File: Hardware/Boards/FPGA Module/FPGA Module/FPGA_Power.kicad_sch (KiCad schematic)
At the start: 1 part, among them U1 XCKU3P-FFVA676

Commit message: Added FPGA Config page
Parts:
- removed U1: XCKU3P-FFVA676, DICE_FPGA_Module:BGA676, symbol DICE_FPGA_Module:XCKU3P-FFVA676
- added U1: XCKU3P-FFVA676, FPGA Module:BGA676, symbol FPGA Module:XCKU3P-FFVA676
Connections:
- new net: U1.AD10 (NC), U1.AE13 (NC), U1.E24 (NC), U1.E25 (NC), U1.E26 (NC), U1.F22 (NC), U1.F23 (NC), U1.F24 (NC), U1.F25 (NC), U1.G20 (NC), U1.G21 (NC), U1.G22 (NC), U1.G24 (NC), U1.G25 (NC), U1.G26 (NC), U1.H19 (NC), U1.H21 (NC), U1.H22 (NC), U1.H23 (NC), U1.H24 (NC), U1.H25 (NC), U1.H26 (NC), U1.J19 (NC), U1.J20 (NC), U1.J21 (NC), U1.J22 (NC), U1.J23 (NC), U1.J24 (NC), U1.J25 (NC), U1.J26 (NC), U1.K18 (NC), U1.K19 (NC), U1.K20 (NC), U1.K21 (NC), U1.K22 (NC), U1.K23 (NC), U1.K25 (NC), U1.K26 (NC), U1.L18 (NC), U1.L19 (NC), U1.L20 (NC), U1.L22 (NC), U1.L23 (NC), U1.L24 (NC), U1.L25 (NC), U1.L26 (NC), U1.M19 (NC), U1.M20 (NC), U1.M21 (NC), U1.M22 (NC), U1.M23 (NC), U1.M24 (NC), U1.M25 (NC), U1.M26 (NC), U1.N18 (NC), U1.N19 (NC), U1.N20 (NC), U1.N21 (NC), U1.N22 (NC), U1.N23 (NC), U1.N24 (NC), U1.N26 (NC), U1.V14 (NC), U1.Y12 (NC), U1.Y13 (NC)
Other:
- note added: "HDMI"

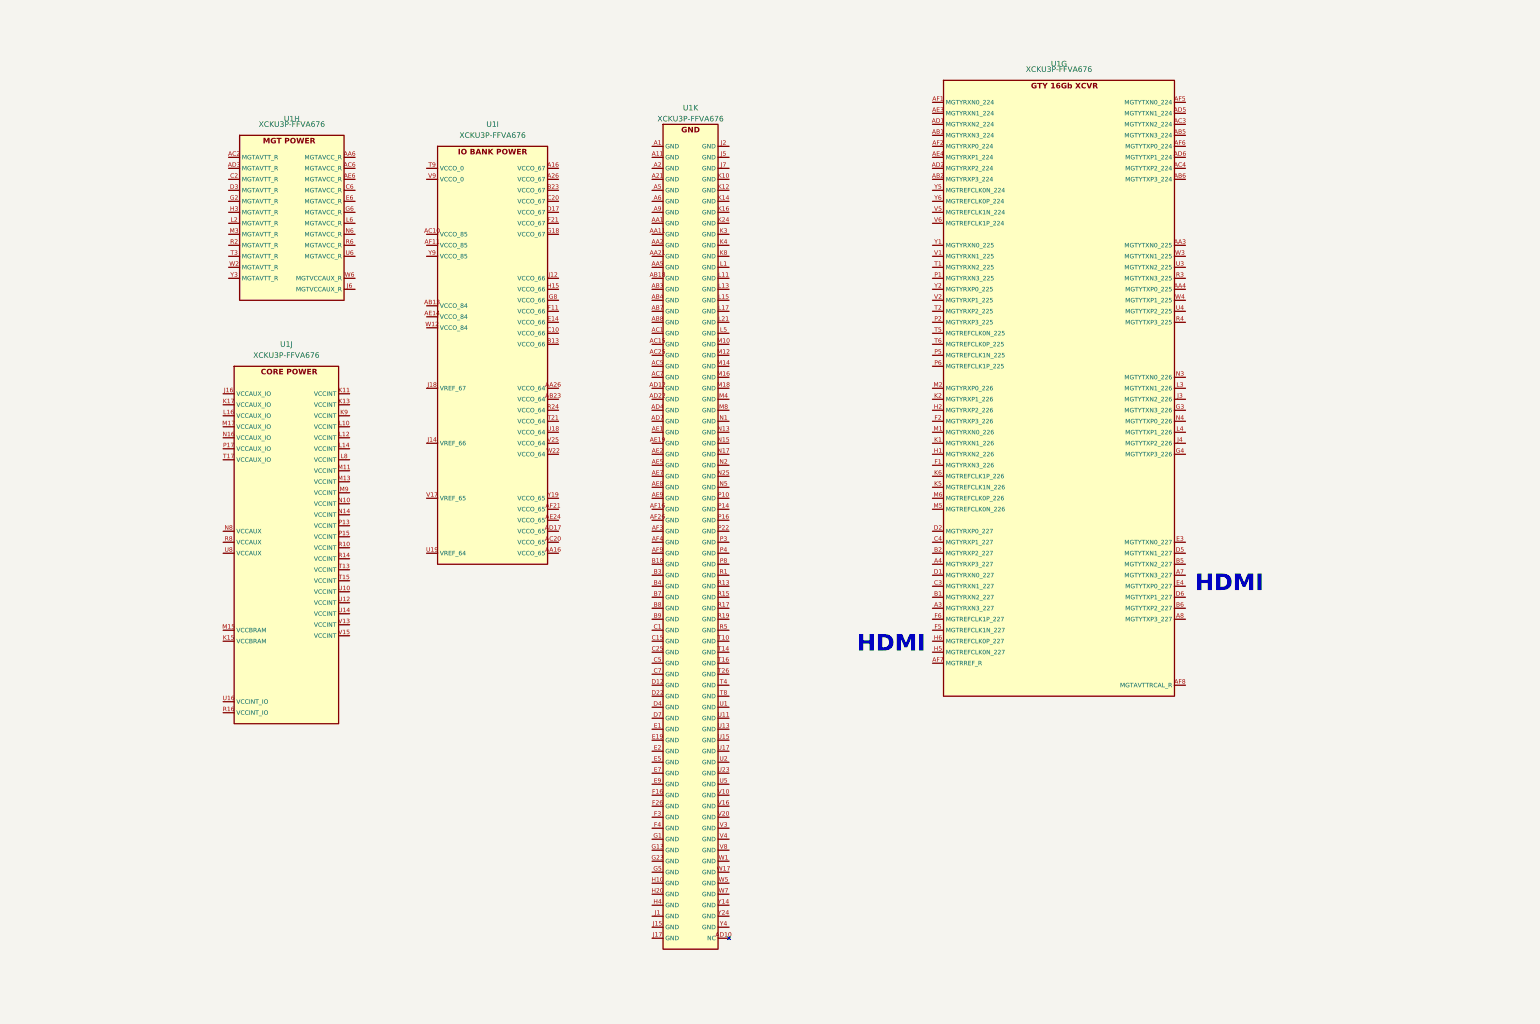
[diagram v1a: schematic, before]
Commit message: Using new DP to HDMI IC
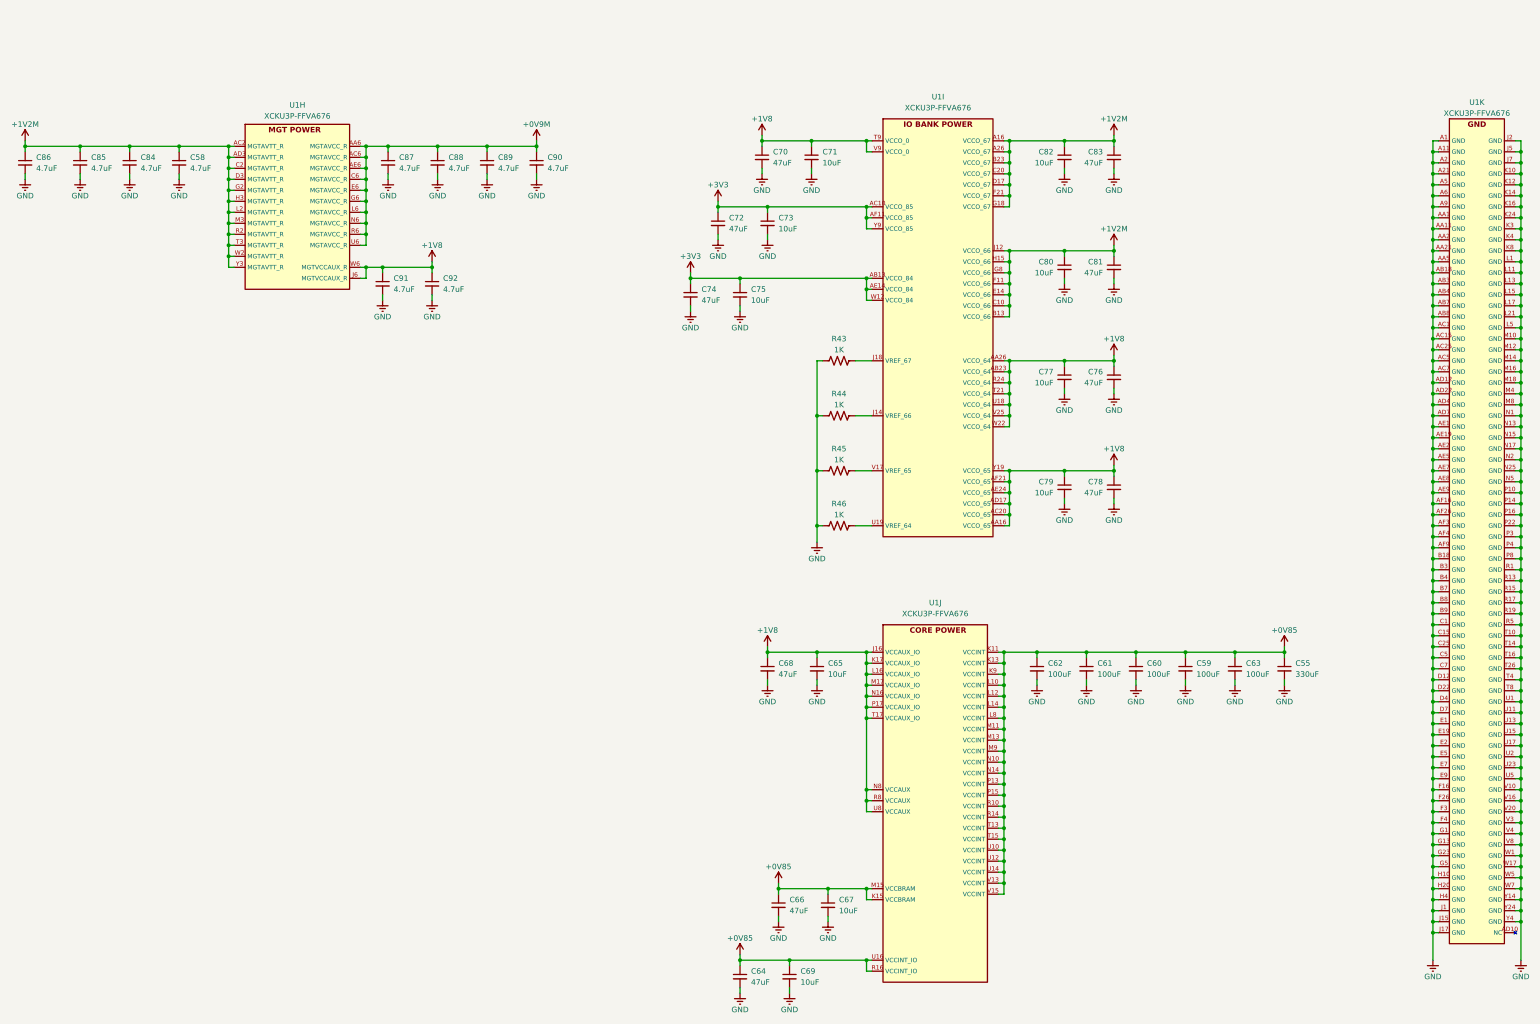
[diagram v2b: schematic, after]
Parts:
- removed unit 7 of U1
- added C55: 330uF, Capacitor_SMD:C_1210_3225Metric, symbol Device:C_Small
- added C58, C84, C85, C86, C87, C88, C89, C90, C91, C92: 4.7uF, Capacitor_SMD:C_0402_1005Metric, symbol Device:C_Small
- added C59, C60, C61, C62, C63: 100uF, Capacitor_SMD:C_0805_2012Metric, symbol Device:C_Small
- added C64, C66, C68, C70, C72, C74, C76, C78, C81, C83: 47uF, Capacitor_SMD:C_0603_1608Metric, symbol Device:C_Small
- added C65, C67, C69, C71, C73, C75, C77, C79, C80, C82: 10uF, Capacitor_SMD:C_0402_1005Metric, symbol Device:C_Small
- added R43, R44, R45, R46: 1K, Resistor_SMD:R_0402_1005Metric, symbol Device:R_US
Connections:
- net +1V2M: now reaches U1.A16 (VCCO_67)
- net +1V2M: now also U1.A26 (VCCO_67), U1.AC2 (MGTAVTT_R), U1.AD3 (MGTAVTT_R), U1.B13 (VCCO_66), U1.B23 (VCCO_67), U1.C10 (VCCO_66), U1.C2 (MGTAVTT_R), U1.C20 (VCCO_67), U1.D17 (VCCO_67), U1.D3 (MGTAVTT_R), U1.E14 (VCCO_66), U1.F11 (VCCO_66), U1.F21 (VCCO_67), U1.G18 (VCCO_67), U1.G2 (MGTAVTT_R), U1.G8 (VCCO_66), U1.H15 (VCCO_66), U1.H3 (MGTAVTT_R), U1.J12 (VCCO_66), U1.L2 (MGTAVTT_R), U1.M3 (MGTAVTT_R), U1.R2 (MGTAVTT_R), U1.T3 (MGTAVTT_R), U1.W2 (MGTAVTT_R), U1.Y3 (MGTAVTT_R), C58.1, C80.1, C81.1, C82.1, C83.1, C84.1, C85.1, C86.1
- net +1V8: now reaches U1.AA16 (VCCO_65)
- net +1V8: now also U1.AA26 (VCCO_64), U1.AB23 (VCCO_64), U1.AC20 (VCCO_65), U1.AD17 (VCCO_65), U1.AE24 (VCCO_65), U1.AF21 (VCCO_65), U1.J16 (VCCAUX_IO), U1.J6 (MGTVCCAUX_R), U1.K17 (VCCAUX_IO), U1.L16 (VCCAUX_IO), U1.M17 (VCCAUX_IO), U1.N16 (VCCAUX_IO), U1.N8 (VCCAUX), U1.P17 (VCCAUX_IO), U1.R24 (VCCO_64), U1.R8 (VCCAUX), U1.T17 (VCCAUX_IO), U1.T21 (VCCO_64), U1.T9 (VCCO_0), U1.U18 (VCCO_64), U1.U8 (VCCAUX), U1.V25 (VCCO_64), U1.V9 (VCCO_0), U1.W22 (VCCO_64), U1.W6 (MGTVCCAUX_R), U1.Y19 (VCCO_65), C65.1, C68.1, C70.1, C71.1, C76.1, C77.1, C78.1, C79.1, C91.1, C92.1
- net +3V3: now reaches U1.AB13 (VCCO_84)
- net +3V3: now also U1.AC10 (VCCO_85), U1.AE14 (VCCO_84), U1.AF11 (VCCO_85), U1.W12 (VCCO_84), U1.Y9 (VCCO_85), C72.1, C73.1, C74.1, C75.1
- net at U1.J14 (VREF_66): now also R44.1
- net at U1.J18 (VREF_67): now also R43.1
- net at U1.U19 (VREF_64): now also R46.1
- net at U1.V17 (VREF_65): now also R45.1
- net +0V85: now reaches U1.K11 (VCCINT)
- net +0V85: now also U1.K13 (VCCINT), U1.K15 (VCCBRAM), U1.K9 (VCCINT), U1.L10 (VCCINT), U1.L12 (VCCINT), U1.L14 (VCCINT), U1.L8 (VCCINT), U1.M11 (VCCINT), U1.M13 (VCCINT), U1.M15 (VCCBRAM), U1.M9 (VCCINT), U1.N10 (VCCINT), U1.N14 (VCCINT), U1.P13 (VCCINT), U1.P15 (VCCINT), U1.R10 (VCCINT), U1.R14 (VCCINT), U1.R16 (VCCINT_IO), U1.T13 (VCCINT), U1.T15 (VCCINT), U1.U10 (VCCINT), U1.U12 (VCCINT), U1.U14 (VCCINT), U1.U16 (VCCINT_IO), U1.V13 (VCCINT), U1.V15 (VCCINT), C55.1, C59.1, C60.1, C61.1, C62.1, C63.1, C64.1, C66.1, C67.1, C69.1
- net GND: now reaches U1.A1 (GND)
- net GND: now also U1.A11 (GND), U1.A2 (GND), U1.A21 (GND), U1.A5 (GND), U1.A6 (GND), U1.A9 (GND), U1.AA1 (GND), U1.AA11 (GND), U1.AA2 (GND), U1.AA21 (GND), U1.AA5 (GND), U1.AB18 (GND), U1.AB3 (GND), U1.AB4 (GND), U1.AB7 (GND), U1.AB8 (GND), U1.AC1 (GND), U1.AC15 (GND), U1.AC25 (GND), U1.AC5 (GND), U1.AC7 (GND), U1.AD12 (GND), U1.AD22 (GND), U1.AD4 (GND), U1.AD7 (GND), U1.AE1 (GND), U1.AE19 (GND), U1.AE2 (GND), U1.AE5 (GND), U1.AE7 (GND), U1.AE8 (GND), U1.AE9 (GND), U1.AF16 (GND), U1.AF26 (GND), U1.AF3 (GND), U1.AF4 (GND), U1.AF9 (GND), U1.B18 (GND), U1.B3 (GND), U1.B4 (GND), U1.B7 (GND), U1.B8 (GND), U1.B9 (GND), U1.C1 (GND), U1.C15 (GND), U1.C25 (GND), U1.C5 (GND), U1.C7 (GND), U1.D12 (GND), U1.D22 (GND), U1.D4 (GND), U1.D7 (GND), U1.E1 (GND), U1.E19 (GND), U1.E2 (GND), U1.E5 (GND), U1.E7 (GND), U1.E9 (GND), U1.F16 (GND), U1.F26 (GND), U1.F3 (GND), U1.F4 (GND), U1.G1 (GND), U1.G13 (GND), U1.G23 (GND), U1.G5 (GND), U1.H10 (GND), U1.H20 (GND), U1.H4 (GND), U1.J1 (GND), U1.J15 (GND), U1.J17 (GND), U1.J2 (GND), U1.J5 (GND), U1.J7 (GND), U1.K10 (GND), U1.K12 (GND), U1.K14 (GND), U1.K16 (GND), U1.K24 (GND), U1.K3 (GND), U1.K4 (GND), U1.K8 (GND), U1.L1 (GND), U1.L11 (GND), U1.L13 (GND), U1.L15 (GND), U1.L17 (GND), U1.L21 (GND), U1.L5 (GND), U1.M10 (GND), U1.M12 (GND), U1.M14 (GND), U1.M16 (GND), U1.M18 (GND), U1.M4 (GND), U1.M8 (GND), U1.N1 (GND), U1.N13 (GND), U1.N15 (GND), U1.N17 (GND), U1.N2 (GND), U1.N25 (GND), U1.N5 (GND), U1.P10 (GND), U1.P14 (GND), U1.P16 (GND), U1.P22 (GND), U1.P3 (GND), U1.P4 (GND), U1.P8 (GND), U1.R1 (GND), U1.R13 (GND), U1.R15 (GND), U1.R17 (GND), U1.R19 (GND), U1.R5 (GND), U1.T10 (GND), U1.T14 (GND), U1.T16 (GND), U1.T26 (GND), U1.T4 (GND), U1.T8 (GND), U1.U1 (GND), U1.U11 (GND), U1.U13 (GND), U1.U15 (GND), U1.U17 (GND), U1.U2 (GND), U1.U23 (GND), U1.U5 (GND), U1.V10 (GND), U1.V16 (GND), U1.V20 (GND), U1.V3 (GND), U1.V4 (GND), U1.V8 (GND), U1.W1 (GND), U1.W17 (GND), U1.W5 (GND), U1.W7 (GND), U1.Y14 (GND), U1.Y24 (GND), U1.Y4 (GND), C55.2, C58.2, C59.2, C60.2, C61.2, C62.2, C63.2, C64.2, C65.2, C66.2, C67.2, C68.2, C69.2, C70.2, C71.2, C72.2, C73.2, C74.2, C75.2, C76.2, C77.2, C78.2, C79.2, C80.2, C81.2, C82.2, C83.2, C84.2, C85.2, C86.2, C87.2, C88.2, C89.2, C90.2, C91.2, C92.2, R43.2, R44.2, R45.2, R46.2
- net +0V9M: now reaches U1.AA6 (MGTAVCC_R)
- net +0V9M: now also U1.AC6 (MGTAVCC_R), U1.AE6 (MGTAVCC_R), U1.C6 (MGTAVCC_R), U1.E6 (MGTAVCC_R), U1.G6 (MGTAVCC_R), U1.L6 (MGTAVCC_R), U1.N6 (MGTAVCC_R), U1.R6 (MGTAVCC_R), U1.U6 (MGTAVCC_R), C87.1, C88.1, C89.1, C90.1
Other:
- note removed: "HDMI"
- moved on the sheet: U1H, U1I, U1J, U1K

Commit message: updated fpga module schematics
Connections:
- net +0V9M renamed +0V9
- net +1V2M renamed +1V2
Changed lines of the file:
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@@
 		(rev "1.0")
 		(company "Drexel University")
-		(comment 1 "Designed by Michael Haahr")
+		(comment 1 "Designed by John Hofmeyr")
 	)
 	(junction
@@
 	)
 	(symbol
-		(lib_id "power:GND")
-		(at 53.34 54.61 0)
+		(lib_id "power:+1V2")
+		(at 280.67 44.45 0)
 		(unit 1)
 		(exclude_from_sim no)
@@
 		(on_board yes)
 		(dnp no)
-		(property "Reference" "#PWR0150"
-			(at 53.34 60.96 0)
+		(property "Reference" "#PWR0117"
+			(at 280.67 48.26 0)
 			(effects
 				(font
@@
 			)
 		)
-		(property "Value" "GND"
-			(at 53.34 58.42 0)
+		(property "Value" "+1V2"
+			(at 280.67 40.64 0)
 			(effects
 				(font
@@
 		)
 		(property "Footprint" ""
-			(at 53.34 54.61 0)
+			(at 280.67 44.45 0)
 			(effects
 				(font
@@
 		)
 		(property "Datasheet" ""
-			(at 53.34 54.61 0)
+			(at 280.67 44.45 0)
 			(effects
 				(font
@@
 			)
 		)
-		(property "Description" "Power symbol creates a global label with name \"GND\" , ground"
-			(at 53.34 54.61 0)
+		(property "Description" "Power symbol creates a global label with name \"+1V2\""
+			(at 280.67 44.45 0)
 			(effects
 				(font
@@
 			(project "FPGA Module"
 				(path "/199f10e2-d4b4-4a27-9e84-7b1ce2ae6bf0/0c296310-f788-47f0-8a3f-43c3444563e8/ff43e174-bde2-43ac-b61b-dc2c71092798"
-					(reference "#PWR0150")
+					(reference "#PWR0117")
 					(unit 1)
 				)
@@
 	)
 	(symbol
-		(lib_id "power:VAA")
-		(at 147.32 45.72 0)
+		(lib_id "power:GND")
+		(at 53.34 54.61 0)
 		(unit 1)
 		(exclude_from_sim no)
@@
 		(on_board yes)
 		(dnp no)
-		(property "Reference" "#PWR0117"
-			(at 147.32 49.53 0)
+		(property "Reference" "#PWR0150"
+			(at 53.34 60.96 0)
 			(effects
 				(font
@@
 			)
 		)
-		(property "Value" "+0V9M"
-			(at 147.32 41.91 0)
+		(property "Value" "GND"
+			(at 53.34 58.42 0)
 			(effects
 				(font
@@
 		)
 		(property "Footprint" ""
-			(at 147.32 45.72 0)
+			(at 53.34 54.61 0)
 			(effects
 				(font
@@
 		)
 		(property "Datasheet" ""
-			(at 147.32 45.72 0)
+			(at 53.34 54.61 0)
 			(effects
 				(font
@@
 			)
 		)
-		(property "Description" "Power symbol creates a global label with name \"VAA\""
-			(at 147.32 45.72 0)
+		(property "Description" "Power symbol creates a global label with name \"GND\" , ground"
+			(at 53.34 54.61 0)
 			(effects
 				(font
@@
 			(project "FPGA Module"
 				(path "/199f10e2-d4b4-4a27-9e84-7b1ce2ae6bf0/0c296310-f788-47f0-8a3f-43c3444563e8/ff43e174-bde2-43ac-b61b-dc2c71092798"
-					(reference "#PWR0117")
+					(reference "#PWR0150")
 					(unit 1)
 				)
@@
 	(symbol
 		(lib_id "power:VAA")
-		(at 280.67 69.85 0)
+		(at 147.32 45.72 0)
 		(unit 1)
 		(exclude_from_sim no)
@@
 		(on_board yes)
 		(dnp no)
-		(property "Reference" "#PWR0141"
-			(at 280.67 73.66 0)
+		(property "Reference" "#PWR0257"
+			(at 147.32 49.53 0)
 			(effects
 				(font
@@
 			)
 		)
-		(property "Value" "+1V2M"
-			(at 280.67 66.04 0)
+		(property "Value" "+0V9"
+			(at 147.32 41.91 0)
 			(effects
 				(font
@@
 		)
 		(property "Footprint" ""
-			(at 280.67 69.85 0)
+			(at 147.32 45.72 0)
 			(effects
 				(font
@@
 		)
 		(property "Datasheet" ""
-			(at 280.67 69.85 0)
+			(at 147.32 45.72 0)
 			(effects
 				(font
@@
 		)
 		(property "Description" "Power symbol creates a global label with name \"VAA\""
-			(at 280.67 69.85 0)
+			(at 147.32 45.72 0)
 			(effects
 				(font
@@
 			(project "FPGA Module"
 				(path "/199f10e2-d4b4-4a27-9e84-7b1ce2ae6bf0/0c296310-f788-47f0-8a3f-43c3444563e8/ff43e174-bde2-43ac-b61b-dc2c71092798"
-					(reference "#PWR0141")
+					(reference "#PWR0257")
 					(unit 1)
 				)
@@
 	)
 	(symbol
+		(lib_id "power:+1V2")
+		(at 280.67 69.85 0)
+		(unit 1)
+		(exclude_from_sim no)
+		(in_bom yes)
+		(on_board yes)
+		(dnp no)
+		(property "Reference" "#PWR0141"
+			(at 280.67 73.66 0)
+			(effects
+				(font
+					(size 1.27 1.27)
+				)
+				(hide yes)
+			)
+		)
+		(property "Value" "+1V2"
+			(at 280.67 66.04 0)
+			(effects
+				(font
+					(size 1.27 1.27)
+				)
+			)
+		)
+		(property "Footprint" ""
+			(at 280.67 69.85 0)
+			(effects
+				(font
+					(size 1.27 1.27)
+				)
+				(hide yes)
+			)
+		)
+		(property "Datasheet" ""
+			(at 280.67 69.85 0)
+			(effects
+				(font
+					(size 1.27 1.27)
+				)
+				(hide yes)
+			)
+		)
+		(property "Description" "Power symbol creates a global label with name \"+1V2\""
+			(at 280.67 69.85 0)
+			(effects
+				(font
+					(size 1.27 1.27)
+				)
+				(hide yes)
+			)
+		)
+		(pin "1"
+		)
+		(instances
+			(project "FPGA Module"
+				(path "/199f10e2-d4b4-4a27-9e84-7b1ce2ae6bf0/0c296310-f788-47f0-8a3f-43c3444563e8/ff43e174-bde2-43ac-b61b-dc2c71092798"
+					(reference "#PWR0141")
+					(unit 1)
+				)
+			)
+		)
+	)
+	(symbol
 		(lib_id "Device:C_Small")
 		(at 212.09 167.64 0)
@@
 	)
 	(symbol
-		(lib_id "power:GND")
-		(at 41.91 54.61 0)
+		(lib_id "power:+1V2")
+		(at 29.21 45.72 0)
 		(unit 1)
 		(exclude_from_sim no)
@@
 		(on_board yes)
 		(dnp no)
-		(property "Reference" "#PWR0148"
-			(at 41.91 60.96 0)
+		(property "Reference" "#PWR0119"
+			(at 29.21 49.53 0)
 			(effects
 				(font
@@
 			)
 		)
-		(property "Value" "GND"
-			(at 41.91 58.42 0)
+		(property "Value" "+1V2"
+			(at 29.21 41.91 0)
 			(effects
 				(font
@@
 		)
 		(property "Footprint" ""
-			(at 41.91 54.61 0)
+			(at 29.21 45.72 0)
 			(effects
 				(font
@@
 		)
 		(property "Datasheet" ""
-			(at 41.91 54.61 0)
+			(at 29.21 45.72 0)
 			(effects
 				(font
@@
 			)
 		)
-		(property "Description" "Power symbol creates a global label with name \"GND\" , ground"
-			(at 41.91 54.61 0)
+		(property "Description" "Power symbol creates a global label with name \"+1V2\""
+			(at 29.21 45.72 0)
 			(effects
 				(font
@@
 			(project "FPGA Module"
 				(path "/199f10e2-d4b4-4a27-9e84-7b1ce2ae6bf0/0c296310-f788-47f0-8a3f-43c3444563e8/ff43e174-bde2-43ac-b61b-dc2c71092798"
-					(reference "#PWR0148")
+					(reference "#PWR0119")
 					(unit 1)
 				)
@@
 	)
 	(symbol
-		(lib_id "power:VAA")
-		(at 280.67 44.45 0)
+		(lib_id "power:GND")
+		(at 41.91 54.61 0)
 		(unit 1)
 		(exclude_from_sim no)
@@
 		(on_board yes)
 		(dnp no)
-		(property "Reference" "#PWR0144"
-			(at 280.67 48.26 0)
+		(property "Reference" "#PWR0148"
+			(at 41.91 60.96 0)
 			(effects
 				(font
@@
 			)
 		)
-		(property "Value" "+1V2M"
-			(at 280.67 40.64 0)
+		(property "Value" "GND"
+			(at 41.91 58.42 0)
 			(effects
 				(font
@@
 		)
 		(property "Footprint" ""
-			(at 280.67 44.45 0)
+			(at 41.91 54.61 0)
 			(effects
 				(font
@@
 		)
 		(property "Datasheet" ""
-			(at 280.67 44.45 0)
+			(at 41.91 54.61 0)
 			(effects
 				(font
@@
 			)
 		)
-		(property "Description" "Power symbol creates a global label with name \"VAA\""
-			(at 280.67 44.45 0)
+		(property "Description" "Power symbol creates a global label with name \"GND\" , ground"
+			(at 41.91 54.61 0)
 			(effects
 				(font
@@
 			(project "FPGA Module"
 				(path "/199f10e2-d4b4-4a27-9e84-7b1ce2ae6bf0/0c296310-f788-47f0-8a3f-43c3444563e8/ff43e174-bde2-43ac-b61b-dc2c71092798"
-					(reference "#PWR0144")
+					(reference "#PWR0148")
 					(unit 1)
 				)
@@
 					(unit 1)
 				)
-			)
-		)
-	)
-	(symbol
-		(lib_id "power:VAA")
-		(at 29.21 45.72 0)
-		(unit 1)
-		(exclude_from_sim no)
-		(in_bom yes)
-		(on_board yes)
-		(dnp no)
-		(property "Reference" "#PWR0119"
-			(at 29.21 49.53 0)
-			(effects
-				(font
-					(size 1.27 1.27)
-				)
-				(hide yes)
-			)
-		)
-		(property "Value" "+1V2M"
-			(at 29.21 41.91 0)
-			(effects
-				(font
-					(size 1.27 1.27)
-				)
-			)
-		)
-		(property "Footprint" ""
-			(at 29.21 45.72 0)
-			(effects
-				(font
-					(size 1.27 1.27)
-				)
-				(hide yes)
-			)
-		)
-		(property "Datasheet" ""
-			(at 29.21 45.72 0)
-			(effects
-				(font
-					(size 1.27 1.27)
-				)
-				(hide yes)
-			)
-		)
-		(property "Description" "Power symbol creates a global label with name \"VAA\""
-			(at 29.21 45.72 0)
-			(effects
-				(font
-					(size 1.27 1.27)
-				)
-				(hide yes)
-			)
-		)
-		(pin "1"
-		)
-		(instances
-			(project "FPGA Module"
-				(path "/199f10e2-d4b4-4a27-9e84-7b1ce2ae6bf0/0c296310-f788-47f0-8a3f-43c3444563e8/ff43e174-bde2-43ac-b61b-dc2c71092798"
-					(reference "#PWR0119")
-					(unit 1)
-				)

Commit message: Update FPGA Module Netclasses
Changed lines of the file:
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@@
 		)
 	)
-	(symbol
-		(lib_id "power:GND")
-		(at 354.33 234.95 0)
-		(unit 1)
-		(exclude_from_sim no)
-		(in_bom yes)
-		(on_board yes)
-		(dnp no)
-		(property "Reference" "#PWR0106"
-			(at 354.33 241.3 0)
-			(effects
-				(font
-					(size 1.27 1.27)
-				)
-				(hide yes)
-			)
-		)
-		(property "Value" "GND"
-			(at 354.33 238.76 0)
-			(effects
-				(font
-					(size 1.27 1.27)
-				)
-			)
-		)
-		(property "Footprint" ""
-			(at 354.33 234.95 0)
-			(effects
-				(font
-					(size 1.27 1.27)
-				)
-				(hide yes)
-			)
-		)
-		(property "Datasheet" ""
-			(at 354.33 234.95 0)
-			(effects
-				(font
-					(size 1.27 1.27)
-				)
-				(hide yes)
-			)
-		)
-		(property "Description" "Power symbol creates a global label with name \"GND\" , ground"
-			(at 354.33 234.95 0)
-			(effects
-				(font
-					(size 1.27 1.27)
-				)
-				(hide yes)
-			)
-		)
-		(pin "1"
-		)
-		(instances
-			(project "FPGA Module"
-				(path "/199f10e2-d4b4-4a27-9e84-7b1ce2ae6bf0/0c296310-f788-47f0-8a3f-43c3444563e8/ff43e174-bde2-43ac-b61b-dc2c71092798"
-					(reference "#PWR0106")
-					(unit 1)
-				)
+	(label "GND"
+		(at 354.33 233.68 90)
+		(fields_autoplaced yes)
+		(effects
+			(font
+				(size 1.27 1.27)
 			)
+			(justify left bottom)
 		)
 	)
@@
 	)
 	(symbol
-		(lib_id "power:GND")
-		(at 212.09 138.43 0)
-		(mirror y)
-		(unit 1)
-		(exclude_from_sim no)
-		(in_bom yes)
-		(on_board yes)
-		(dnp no)
-		(property "Reference" "#PWR0147"
-			(at 212.09 144.78 0)
-			(effects
-				(font
-					(size 1.27 1.27)
-				)
-				(hide yes)
-			)
-		)
-		(property "Value" "GND"
-			(at 212.09 142.24 0)
-			(effects
-				(font
-					(size 1.27 1.27)
-				)
-			)
-		)
-		(property "Footprint" ""
-			(at 212.09 138.43 0)
-			(effects
-				(font
-					(size 1.27 1.27)
-				)
-				(hide yes)
-			)
-		)
-		(property "Datasheet" ""
-			(at 212.09 138.43 0)
-			(effects
-				(font
-					(size 1.27 1.27)
-				)
-				(hide yes)
-			)
-		)
-		(property "Description" "Power symbol creates a global label with name \"GND\" , ground"
-			(at 212.09 138.43 0)
-			(effects
-				(font
-					(size 1.27 1.27)
-				)
-				(hide yes)
-			)
-		)
-		(pin "1"
-		)
-		(instances
-			(project "FPGA Module"
-				(path "/199f10e2-d4b4-4a27-9e84-7b1ce2ae6bf0/0c296310-f788-47f0-8a3f-43c3444563e8/ff43e174-bde2-43ac-b61b-dc2c71092798"
-					(reference "#PWR0147")
-					(unit 1)
-				)
-			)
-		)
-	)
-	(symbol
 		(lib_id "power:+1V2")
 		(at 280.67 69.85 0)
@@
 	)
 	(symbol
+		(lib_id "power:GND")
+		(at 212.09 138.43 0)
+		(mirror y)
+		(unit 1)
+		(exclude_from_sim no)
+		(in_bom yes)
+		(on_board yes)
+		(dnp no)
+		(property "Reference" "#PWR023"
+			(at 212.09 144.78 0)
+			(effects
+				(font
+					(size 1.27 1.27)
+				)
+				(hide yes)
+			)
+		)
+		(property "Value" "GND"
+			(at 212.09 142.24 0)
+			(effects
+				(font
+					(size 1.27 1.27)
+				)
+			)
+		)
+		(property "Footprint" ""
+			(at 212.09 138.43 0)
+			(effects
+				(font
+					(size 1.27 1.27)
+				)
+				(hide yes)
+			)
+		)
+		(property "Datasheet" ""
+			(at 212.09 138.43 0)
+			(effects
+				(font
+					(size 1.27 1.27)
+				)
+				(hide yes)
+			)
+		)
+		(property "Description" "Power symbol creates a global label with name \"GND\" , ground"
+			(at 212.09 138.43 0)
+			(effects
+				(font
+					(size 1.27 1.27)
+				)
+				(hide yes)
+			)
+		)
+		(pin "1"
+		)
+		(instances
+			(project "FPGA Module"
+				(path "/199f10e2-d4b4-4a27-9e84-7b1ce2ae6bf0/0c296310-f788-47f0-8a3f-43c3444563e8/ff43e174-bde2-43ac-b61b-dc2c71092798"
+					(reference "#PWR023")
+					(unit 1)
+				)
+			)
+		)
+	)
+	(symbol
 		(lib_id "Device:C_Small")
 		(at 182.88 81.28 0)
@@
 					(unit 1)
 				)
+			)
+		)
+	)
+	(symbol
+		(lib_id "power:GND")
+		(at 354.33 234.95 0)
+		(unit 1)
+		(exclude_from_sim no)
+		(in_bom yes)
+		(on_board yes)
+		(dnp no)
+		(property "Reference" "#PWR0106"
+			(at 354.33 241.3 0)
+			(effects
+				(font
+					(size 1.27 1.27)
+				)
+				(hide yes)
+			)
+		)
+		(property "Value" "GND"
+			(at 354.33 238.76 0)
+			(effects
+				(font
+					(size 1.27 1.27)
+				)
+			)
+		)
+		(property "Footprint" ""
+			(at 354.33 234.95 0)
+			(effects
+				(font
+					(size 1.27 1.27)
+				)
+				(hide yes)
+			)
+		)
+		(property "Datasheet" ""
+			(at 354.33 234.95 0)
+			(effects
+				(font
+					(size 1.27 1.27)
+				)
+				(hide yes)
+			)
+		)
+		(property "Description" "Power symbol creates a global label with name \"GND\" , ground"
+			(at 354.33 234.95 0)
+			(effects
+				(font
+					(size 1.27 1.27)
+				)
+				(hide yes)
+			)
+		)
+		(pin "1"
+		)
+		(instances
+			(project "FPGA Module"
+				(path "/199f10e2-d4b4-4a27-9e84-7b1ce2ae6bf0/0c296310-f788-47f0-8a3f-43c3444563e8/ff43e174-bde2-43ac-b61b-dc2c71092798"
+					(reference "#PWR0106")
+					(unit 1)
+				)
